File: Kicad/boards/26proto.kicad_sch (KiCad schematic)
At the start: 46 parts, among them J1 5051104096, J10 Conn_01x05, J2 Micro_SD_Card, J3 URM37, J4 RE12A, J5 RS485_TFT, J6 RS485_airdata, J7 RS485_logger_2, J8 RS485_logger, J9 BNO085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

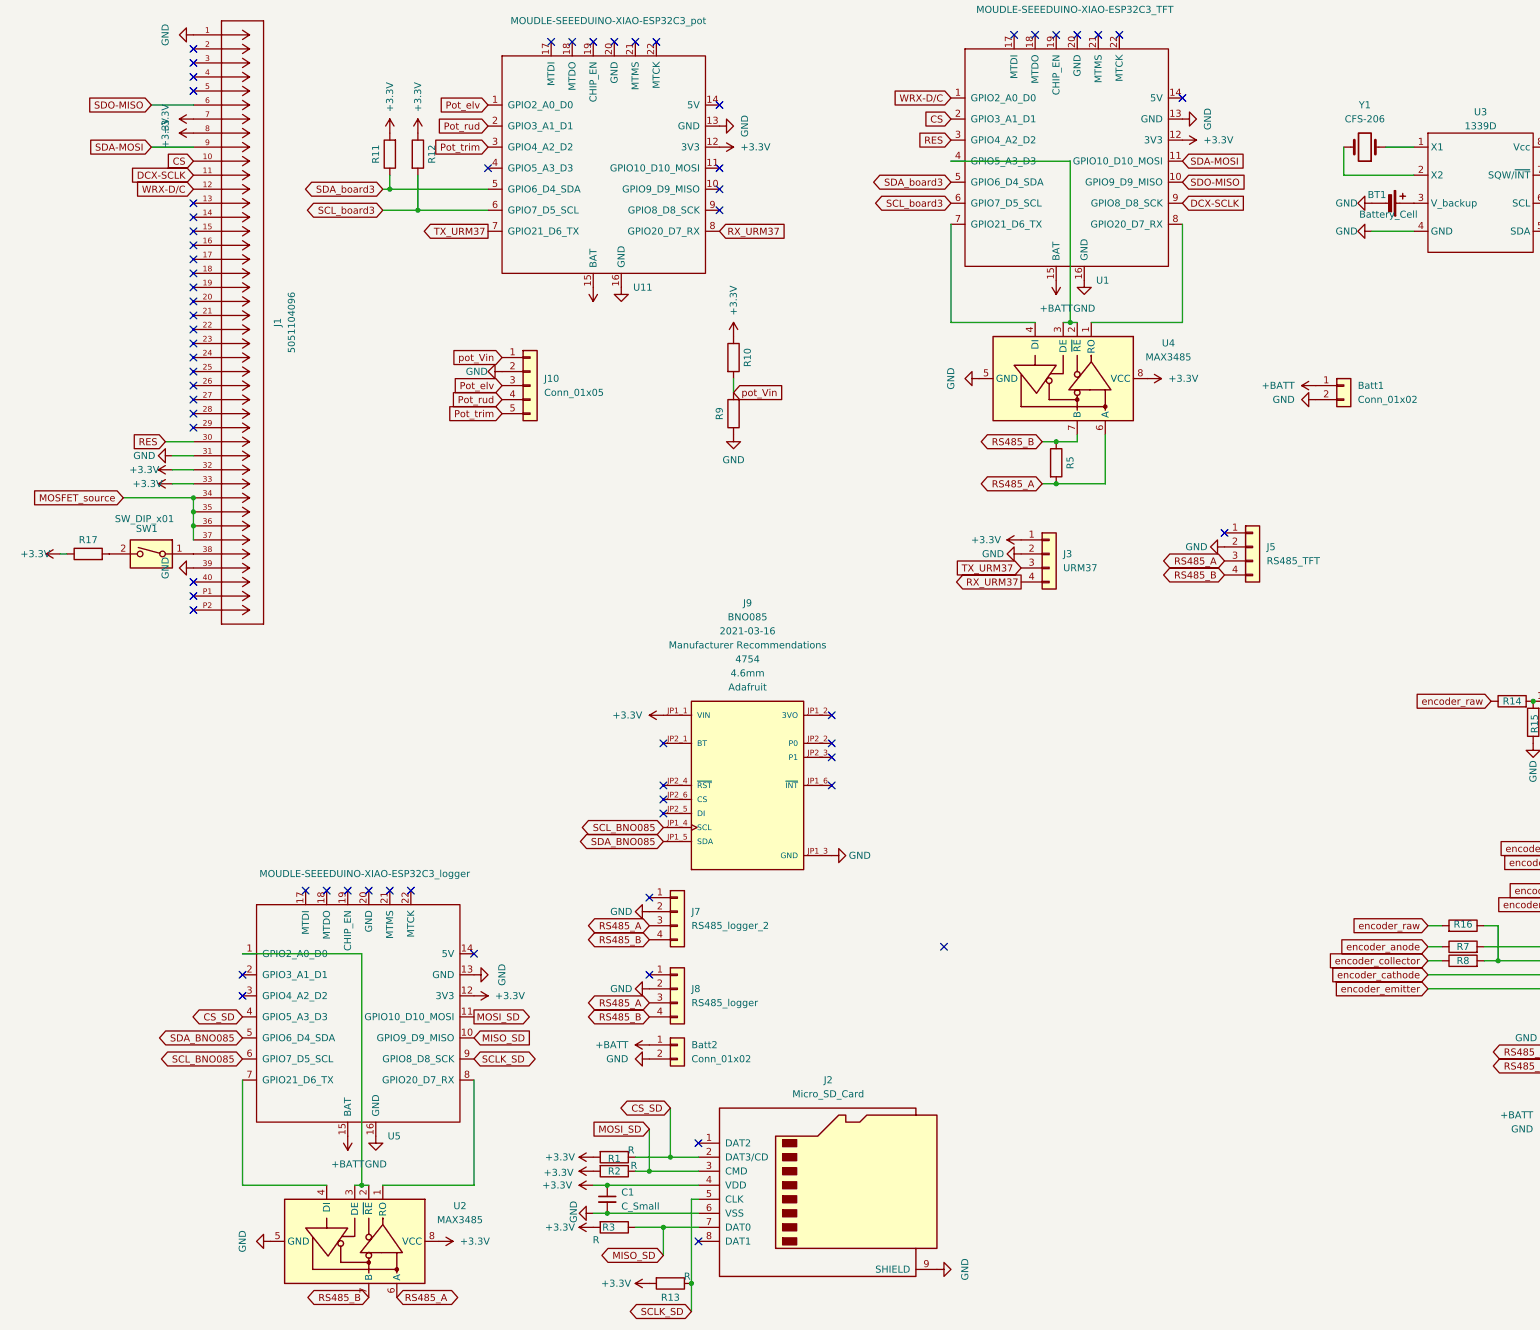
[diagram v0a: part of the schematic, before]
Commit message: add resister values
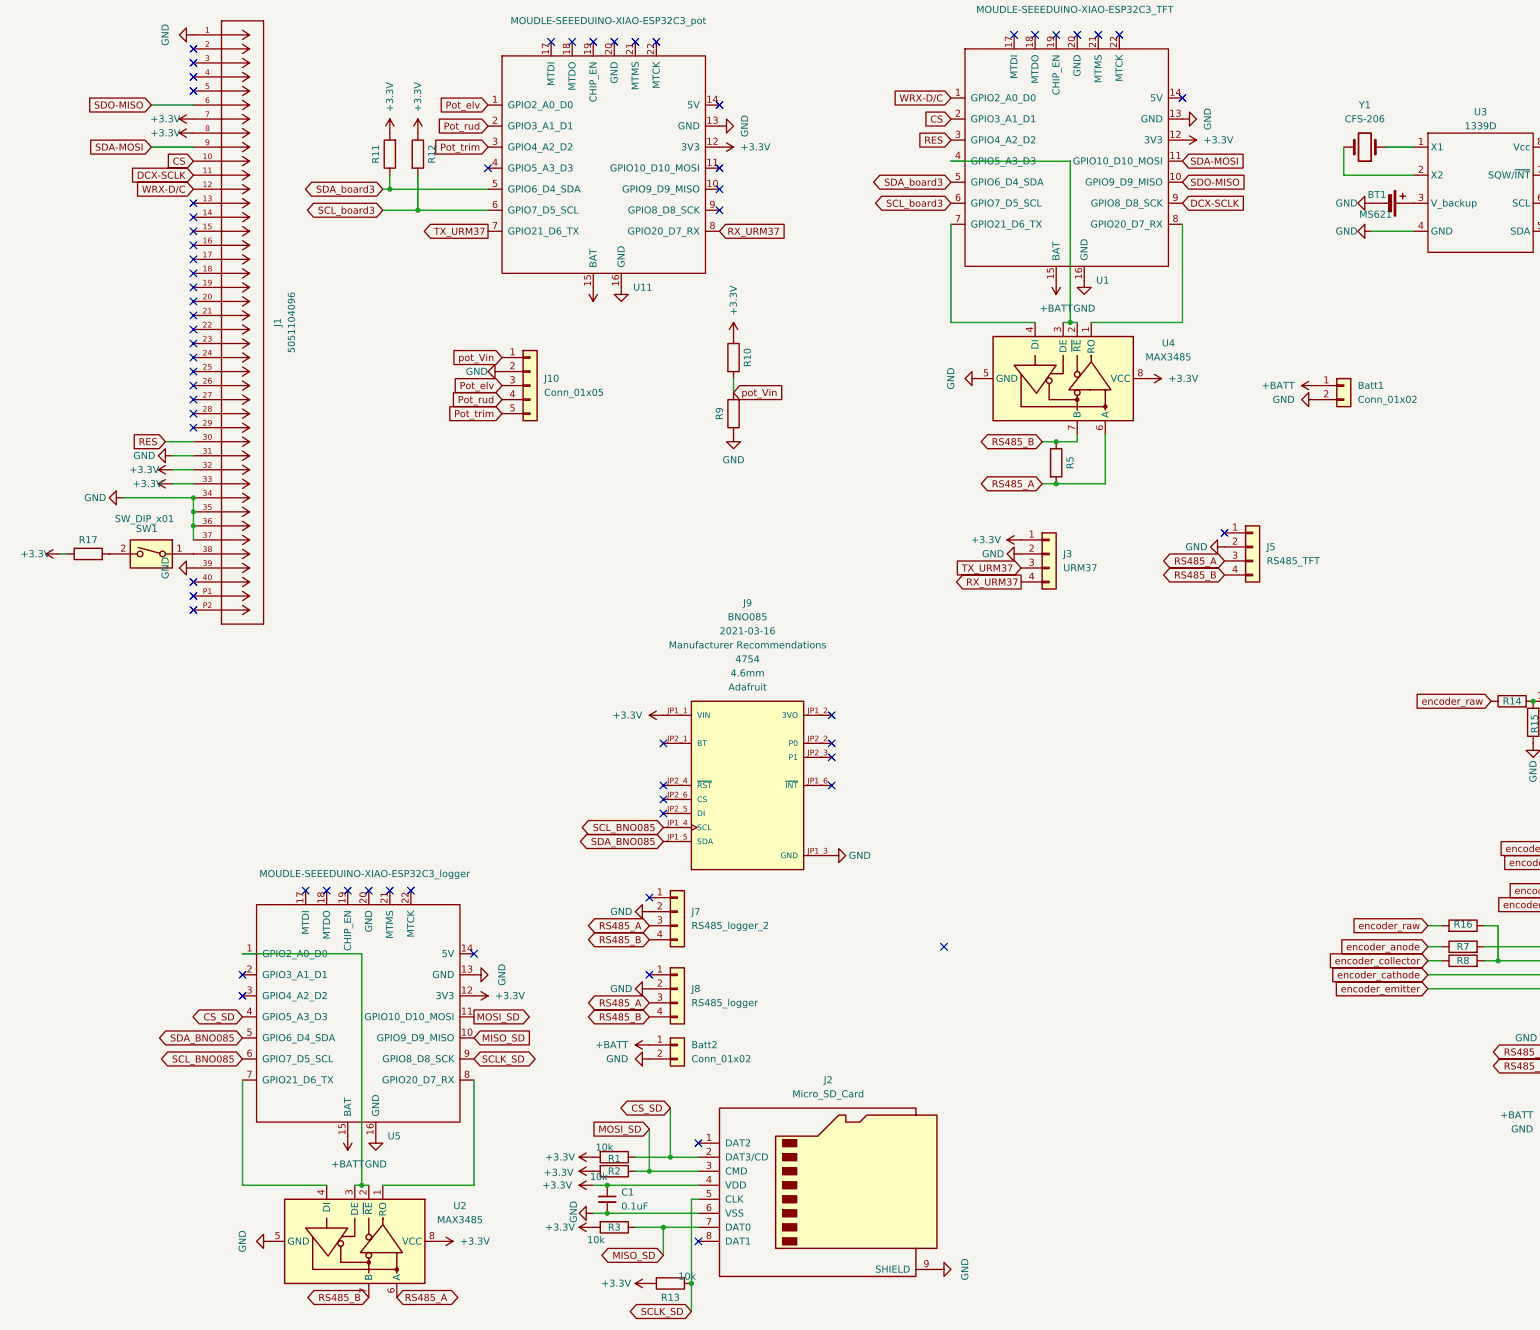
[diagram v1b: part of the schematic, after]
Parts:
- BT1: value Battery_Cell -> MS621
- C1: value C_Small -> 0.1uF
- R1, R13, R14, R16, R2, R3, R6: value R -> 10k
- R11, R12: value R -> 3.3k
- R15: value R -> 100k
- R17: value R -> 10
- R4, R5: value R -> 120
- R7: value R -> 330
- R8: value R -> 3k
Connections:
- net MOSFET_source is gone; now on net GND: J1.34, J1.35, J1.36, J1.37
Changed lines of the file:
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@@
 		)
 	)
-	(global_label "MOSFET_source"
-		(shape input)
-		(at 33.02 109.22 180)
-		(fields_autoplaced yes)
-		(effects
-			(font
-				(size 1.27 1.27)
-			)
-			(justify right)
-		)
-		(property "Intersheetrefs" "${INTERSHEET_REFS}"
-			(at 15.5811 109.22 0)
-			(effects
-				(font
-					(size 1.27 1.27)
-				)
-				(justify right)
-				(hide yes)
-			)
-		)
-	)
 	(global_label "SCL_BNO085"
 		(shape bidirectional)
@@
 			)
 		)
-		(property "Value" "R"
+		(property "Value" "10k"
 			(at 294.64 131.572 90)
 			(effects
@@
 		(on_board yes)
 		(dnp no)
-		(fields_autoplaced yes)
 		(property "Reference" "#PWR07"
 			(at 49.53 43.18 0)
@@
 		)
 		(property "Value" "+3.3V"
-			(at 40.64 43.18 0)
+			(at 40.64 43.18 90)
 			(effects
 				(font
@@
 			)
 		)
-		(property "Value" "C_Small"
+		(property "Value" "0.1uF"
 			(at 123.19 237.4962 0)
 			(effects
@@
 		(dnp no)
 		(property "Reference" "R3"
-			(at 120.904 241.3 90)
+			(at 121.92 241.3 90)
 			(effects
 				(font
@@
 			)
 		)
-		(property "Value" "R"
+		(property "Value" "10k"
 			(at 118.618 243.586 90)
 			(effects
@@
 			)
 		)
-		(property "Value" "R"
-			(at 125.476 230.124 90)
+		(property "Value" "10k"
+			(at 119.126 232.156 90)
 			(effects
 				(font
@@
 			)
 		)
-		(property "Value" "R"
-			(at 124.968 227.33 90)
+		(property "Value" "10k"
+			(at 120.142 226.822 90)
 			(effects
 				(font
@@
 			)
 		)
-		(property "Value" "R"
+		(property "Value" "3.3k"
 			(at 82.55 50.038 90)
 			(effects
@@
 			)
 		)
-		(property "Value" "R"
+		(property "Value" "120"
 			(at 200.66 99.822 90)
 			(effects
@@
 			)
 		)
-		(property "Value" "R"
+		(property "Value" "10k"
 			(at 281.432 147.32 90)
 			(effects
@@
 			)
 		)
-		(property "Value" "R"
+		(property "Value" "10"
 			(at 23.622 120.65 90)
 			(effects
@@
 			)
 		)
-		(property "Value" "Battery_Cell"
+		(property "Value" "MS621"
 			(at 256.794 57.912 90)
 			(effects
@@
 			)
 		)
-		(property "Value" "R"
+		(property "Value" "120"
 			(at 354.33 200.152 90)
 			(effects
@@
 	)
 	(symbol
+		(lib_id "power:GND")
+		(at 33.02 109.22 270)
+		(mirror x)
+		(unit 1)
+		(exclude_from_sim no)
+		(in_bom yes)
+		(on_board yes)
+		(dnp no)
+		(property "Reference" "#PWR09"
+			(at 26.67 109.22 0)
+			(effects
+				(font
+					(size 1.27 1.27)
+				)
+				(hide yes)
+			)
+		)
+		(property "Value" "GND"
+			(at 27.94 109.22 90)
+			(effects
+				(font
+					(size 1.27 1.27)
+				)
+			)
+		)
+		(property "Footprint" ""
+			(at 33.02 109.22 0)
+			(effects
+				(font
+					(size 1.27 1.27)
+				)
+				(hide yes)
+			)
+		)
+		(property "Datasheet" ""
+			(at 33.02 109.22 0)
+			(effects
+				(font
+					(size 1.27 1.27)
+				)
+				(hide yes)
+			)
+		)
+		(property "Description" "Power symbol creates a global label with name \"GND\" , ground"
+			(at 33.02 109.22 0)
+			(effects
+				(font
+					(size 1.27 1.27)
+				)
+				(hide yes)
+			)
+		)
+		(pin "1"
+		)
+		(instances
+			(project "26proto"
+				(path "/493bec57-bd9f-4f18-b3ef-0d7a091ad475"
+					(reference "#PWR09")
+					(unit 1)
+				)
+			)
+		)
+	)
+	(symbol
 		(lib_id "Device:R")
 		(at 288.29 149.86 180)
@@
 			)
 		)
-		(property "Value" "R"
+		(property "Value" "100k"
 			(at 289.56 152.908 90)
 			(effects
@@
 			)
 		)
-		(property "Value" "R"
+		(property "Value" "10k"
 			(at 278.638 187.96 90)
 			(effects
@@
 		(on_board yes)
 		(dnp no)
-		(fields_autoplaced yes)
 		(property "Reference" "#PWR06"
 			(at 49.53 40.64 0)
@@
 		)
 		(property "Value" "+3.3V"
-			(at 40.64 40.64 0)
+			(at 40.64 40.64 90)
 			(effects
 				(font
@@
 			)
 		)
-		(property "Value" "R"
+		(property "Value" "3.3k"
 			(at 85.09 43.942 90)
 			(effects
@@
 			)
 		)
-		(property "Value" "R"
+		(property "Value" "3k"
 			(at 272.542 194.31 90)
 			(effects
@@
 			)
 		)
-		(property "Value" "R"
+		(property "Value" "10k"
 			(at 135.128 250.19 90)
 			(effects
@@
 			)
 		)
-		(property "Value" "R"
+		(property "Value" "330"
 			(at 272.542 191.77 90)
 			(effects

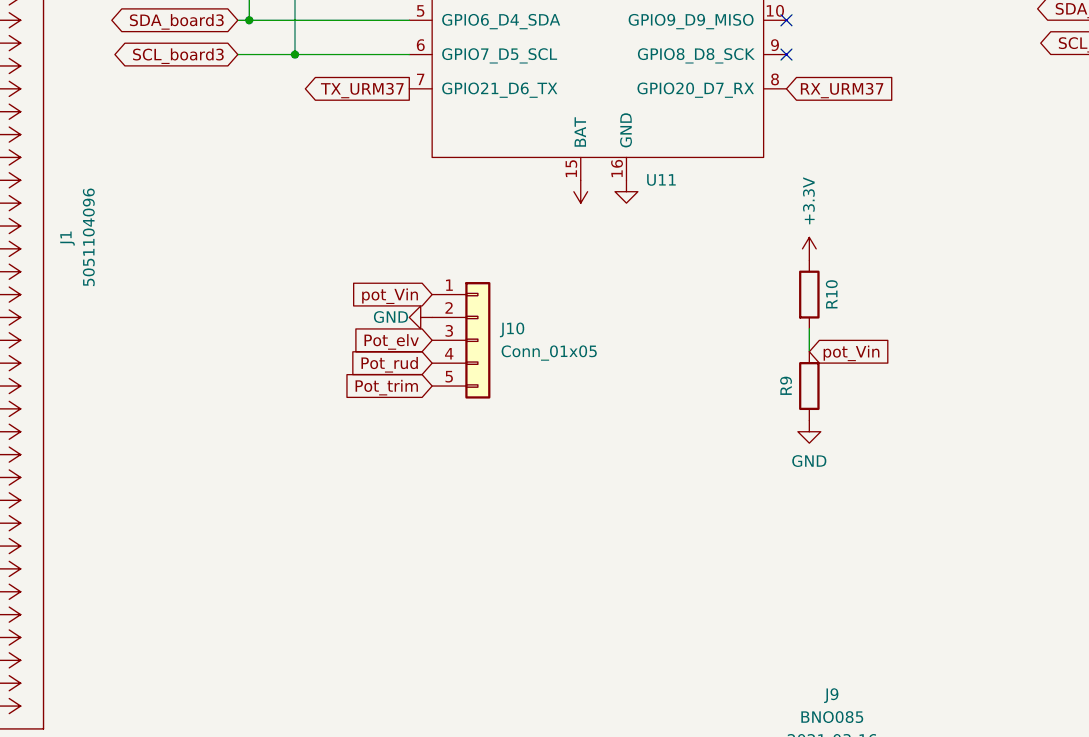
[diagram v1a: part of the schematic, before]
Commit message: add voltage divide resistor
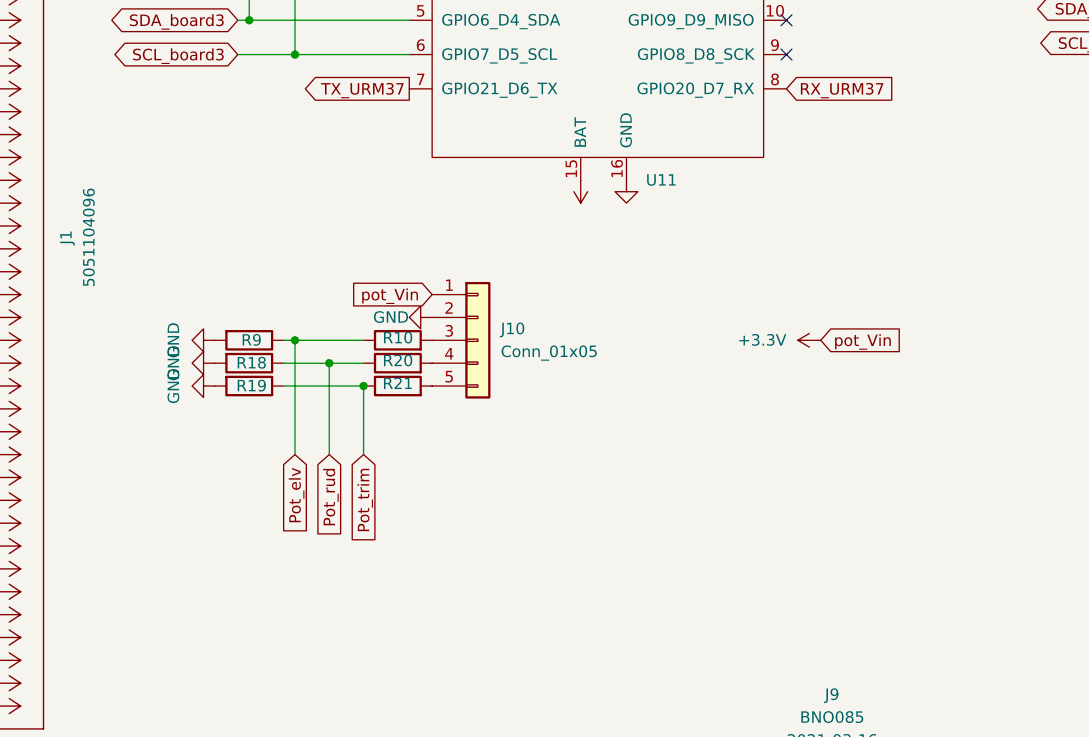
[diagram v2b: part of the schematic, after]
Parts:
- added R18, R19: 10k, Resistor_SMD:R_0603_1608Metric_Pad0.98x0.95mm_HandSolder, symbol Device:R
- added R20, R21: 3.3k, Resistor_SMD:R_0603_1608Metric_Pad0.98x0.95mm_HandSolder, symbol Device:R
- R10: value R -> 3.3k
- R9: value R -> 10k
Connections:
- net +3.3V: now also J10.1 (Pin_1); no longer R10.1
- net GND: now also R9.2, R18.2, R19.2; no longer R9.1
- net Pot_elv: now also R10.1, R9.1; no longer J10.3 (Pin_3)
- net Pot_rud: now also R18.1, R20.1; no longer J10.4 (Pin_4)
- net Pot_trim: now also R19.1, R21.1; no longer J10.5 (Pin_5)
- removed net pot_Vin: J10.1 (Pin_1), R10.2, R9.2
- new net: J10.5 (Pin_5), R21.2
- new net: J10.3 (Pin_3), R10.2
- new net: J10.4 (Pin_4), R20.2
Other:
- moved on the sheet: R10, R9
